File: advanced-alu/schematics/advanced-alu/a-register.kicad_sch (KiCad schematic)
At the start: 11 parts

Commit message: updated ALU design
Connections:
- net GND: now reaches U?.10 (GND)
- net GND: now also U?.8 (GND), U?.8 (GND)
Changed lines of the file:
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@@
     (pin "2")
     (pin "3")
+    (pin "4")
+    (pin "5")
+    (pin "6")
+    (pin "10")
+    (pin "8")
+    (pin "9")
+    (pin "11")
+    (pin "12")
+    (pin "13")
+    (pin "14")
+    (pin "7")
   )
   (symbol (lib_id "74xx:74LS32") (at 153.035 46.355 0) (unit 2)
@@
       (effects (font (size 1.27 1.27)) hide)
     )
-    (pin "4")
-    (pin "5")
-    (pin "6")
+    (pin "1")
+    (pin "2")
+    (pin "3")
+    (pin "4")
+    (pin "5")
+    (pin "6")
+    (pin "10")
+    (pin "8")
+    (pin "9")
+    (pin "11")
+    (pin "12")
+    (pin "13")
+    (pin "14")
+    (pin "7")
   )
   (symbol (lib_id "power:VCC") (at 109.22 93.98 0) (unit 1)
@@
     )
     (property "Datasheet" "" (id 3) (at 109.22 93.98 0)
+      (effects (font (size 1.27 1.27)) hide)
+    )
+    (pin "1")
+  )
+  (symbol (lib_id "power:GND") (at 139.065 93.98 0) (unit 1)
+    (in_bom yes) (on_board yes) (fields_autoplaced)
+    (property "Reference" "#PWR?" (id 0) (at 139.065 100.33 0)
+      (effects (font (size 1.27 1.27)) hide)
+    )
+    (property "Value" "GND" (id 1) (at 139.065 98.5425 0))
+    (property "Footprint" "" (id 2) (at 139.065 93.98 0)
+      (effects (font (size 1.27 1.27)) hide)
+    )
+    (property "Datasheet" "" (id 3) (at 139.065 93.98 0)
       (effects (font (size 1.27 1.27)) hide)
     )
@@
     (pin "1")
     (pin "2")
+    (pin "3")
+    (pin "4")
+    (pin "5")
+    (pin "6")
+    (pin "8")
+    (pin "9")
+    (pin "10")
+    (pin "11")
+    (pin "12")
+    (pin "13")
+    (pin "14")
+    (pin "7")
+  )
+  (symbol (lib_id "power:GND") (at 68.58 93.98 0) (unit 1)
+    (in_bom yes) (on_board yes) (fields_autoplaced)
+    (property "Reference" "#PWR?" (id 0) (at 68.58 100.33 0)
+      (effects (font (size 1.27 1.27)) hide)
+    )
+    (property "Value" "GND" (id 1) (at 68.58 98.5425 0))
+    (property "Footprint" "" (id 2) (at 68.58 93.98 0)
+      (effects (font (size 1.27 1.27)) hide)
+    )
+    (property "Datasheet" "" (id 3) (at 68.58 93.98 0)
+      (effects (font (size 1.27 1.27)) hide)
+    )
+    (pin "1")
   )
   (symbol (lib_id "74xx:74LS08") (at 132.08 43.815 0) (unit 4)
@@
       (effects (font (size 1.27 1.27)) hide)
     )
-    (pin "11")
-    (pin "12")
-    (pin "13")
+    (pin "1")
+    (pin "2")
+    (pin "3")
+    (pin "4")
+    (pin "5")
+    (pin "6")
+    (pin "10")
+    (pin "8")
+    (pin "9")
+    (pin "11")
+    (pin "12")
+    (pin "13")
+    (pin "14")
+    (pin "7")
   )
   (symbol (lib_id "74xx:74LS194") (at 164.465 93.98 270) (unit 1)
@@
     (pin "2")
     (pin "3")
+    (pin "4")
+    (pin "5")
+    (pin "6")
+    (pin "10")
+    (pin "8")
+    (pin "9")
+    (pin "11")
+    (pin "12")
+    (pin "13")
+    (pin "14")
+    (pin "7")
   )
   (symbol (lib_id "74xx:74LS08") (at 116.84 156.845 180) (unit 2)
@@
       (effects (font (size 1.27 1.27)) hide)
     )
-    (pin "4")
-    (pin "5")
-    (pin "6")
+    (pin "1")
+    (pin "2")
+    (pin "3")
+    (pin "4")
+    (pin "5")
+    (pin "6")
+    (pin "10")
+    (pin "8")
+    (pin "9")
+    (pin "11")
+    (pin "12")
+    (pin "13")
+    (pin "14")
+    (pin "7")
   )
   (symbol (lib_id "74xx:74LS08") (at 73.66 137.16 180) (unit 3)
@@
       (effects (font (size 1.27 1.27)) hide)
     )
-    (pin "10")
-    (pin "8")
-    (pin "9")
+    (pin "1")
+    (pin "2")
+    (pin "3")
+    (pin "4")
+    (pin "5")
+    (pin "6")
+    (pin "10")
+    (pin "8")
+    (pin "9")
+    (pin "11")
+    (pin "12")
+    (pin "13")
+    (pin "14")
+    (pin "7")
+  )
+  (symbol (lib_id "power:GND") (at 203.2 93.98 0) (unit 1)
+    (in_bom yes) (on_board yes) (fields_autoplaced)
+    (property "Reference" "#PWR?" (id 0) (at 203.2 100.33 0)
+      (effects (font (size 1.27 1.27)) hide)
+    )
+    (property "Value" "GND" (id 1) (at 203.2 98.5425 0))
+    (property "Footprint" "" (id 2) (at 203.2 93.98 0)
+      (effects (font (size 1.27 1.27)) hide)
+    )
+    (property "Datasheet" "" (id 3) (at 203.2 93.98 0)
+      (effects (font (size 1.27 1.27)) hide)
+    )
+    (pin "1")
   )
   (symbol (lib_id "74xx:74LS32") (at 94.615 151.765 180) (unit 1)
@@
     (pin "2")
     (pin "3")
+    (pin "4")
+    (pin "5")
+    (pin "6")
+    (pin "10")
+    (pin "8")
+    (pin "9")
+    (pin "11")
+    (pin "12")
+    (pin "13")
+    (pin "14")
+    (pin "7")
   )
 )

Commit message: updated documentation
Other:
- title: (none) -> Advanced Arithmetic Logic Unit - Accumulator/Shifter
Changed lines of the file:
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@@
 (kicad_sch (version 20211123) (generator eeschema)
   (paper "A4")
+  (title_block
+    (title "Advanced Arithmetic Logic Unit - Accumulator/Shifter")
+  )
   (junction (at 179.7246 106.68) (diameter 0) (color 0 0 0 0)
   )

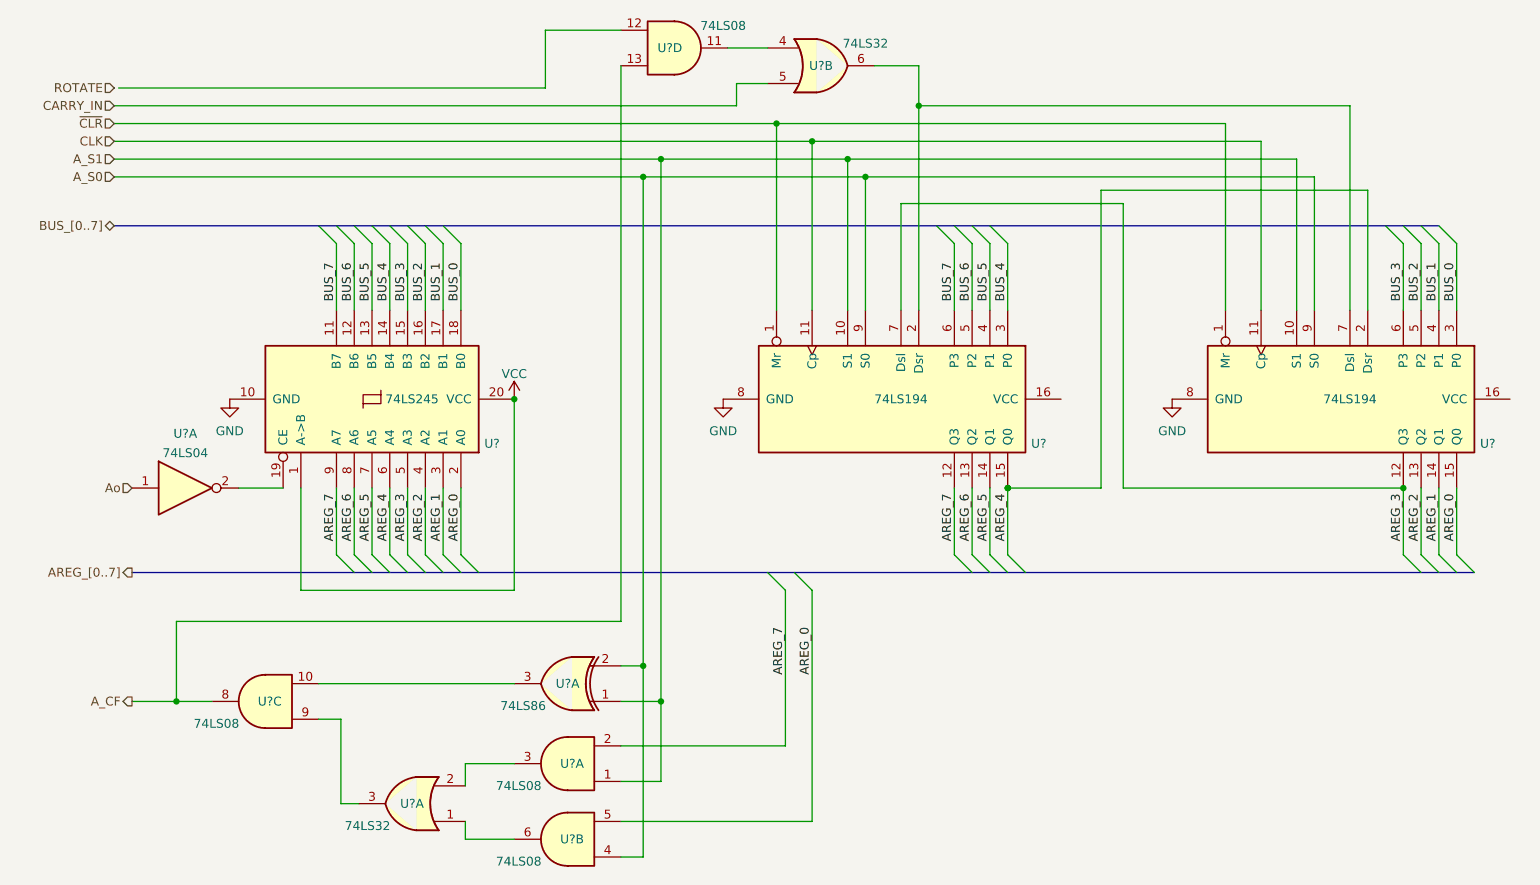
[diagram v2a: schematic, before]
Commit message: returned temp registr to being 8-bit
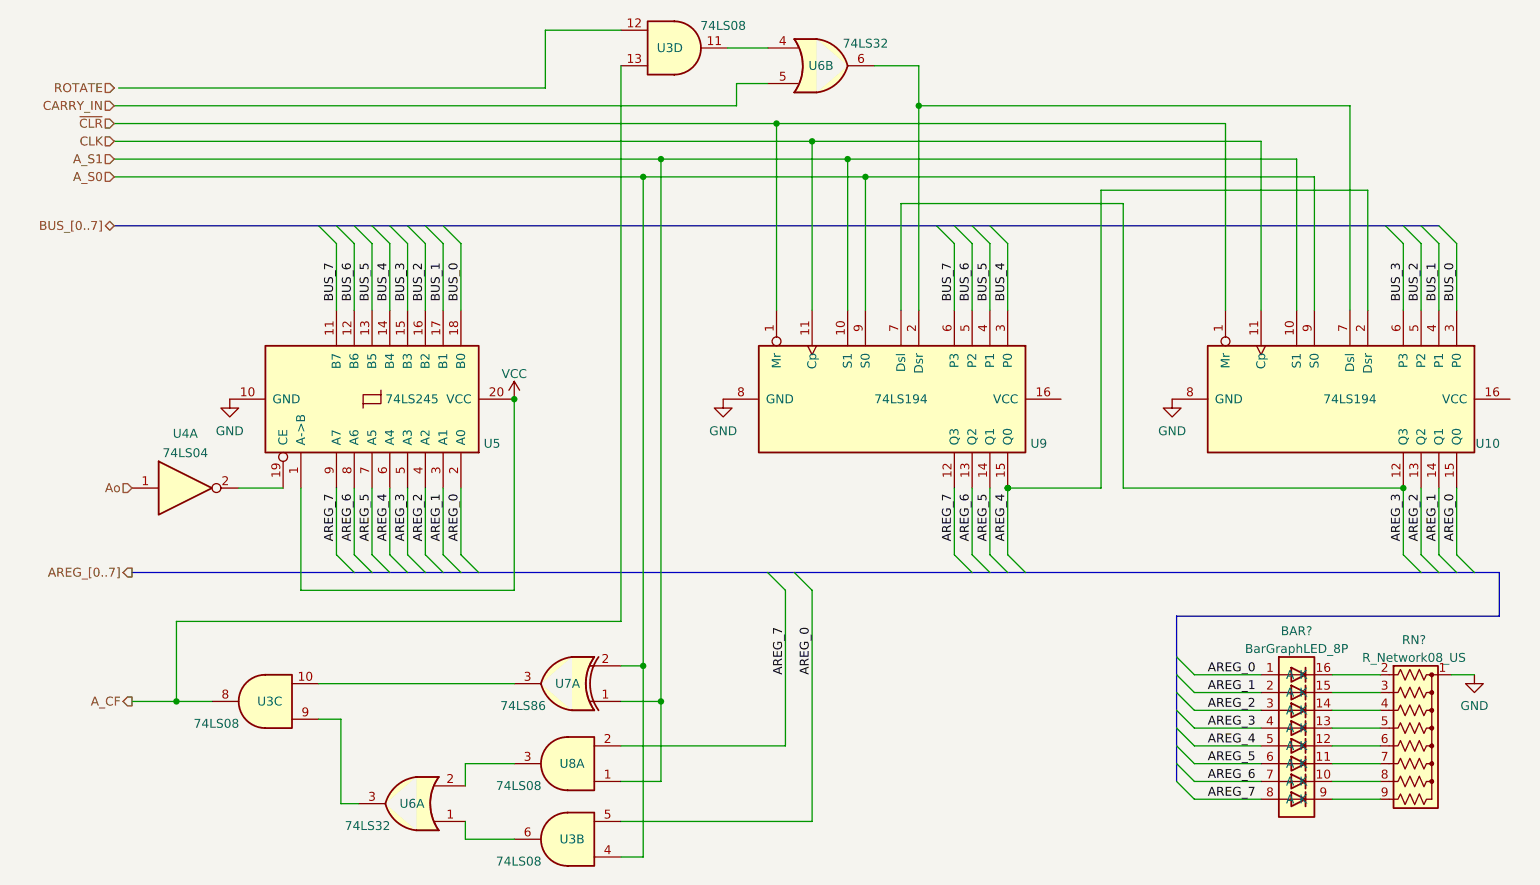
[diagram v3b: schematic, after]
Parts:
- added BAR?: BarGraphLED_8P, symbol common-symbols:BarGraphLED_8P
- added RN?: R_Network08_US, Resistor_THT:R_Array_SIP9, symbol Device:R_Network08_US
- gave numbers to parts that had none: 8
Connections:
- net AREG_0: now also BAR?.1 (A)
- net AREG_1: now also BAR?.2 (A)
- net AREG_2: now also BAR?.3 (A)
- net AREG_3: now also BAR?.4 (A)
- net AREG_4: now also BAR?.5 (A)
- net AREG_5: now also BAR?.6 (A)
- net AREG_6: now also BAR?.7 (A)
- net AREG_7: now also BAR?.8 (A)
- net GND: now also RN?.1 (common)
- new net: BAR?.10 (K), RN?.8 (R7)
- new net: BAR?.11 (K), RN?.7 (R6)
- new net: BAR?.12 (K), RN?.6 (R5)
- new net: BAR?.13 (K), RN?.5 (R4)
- new net: BAR?.14 (K), RN?.4 (R3)
- new net: BAR?.15 (K), RN?.3 (R2)
- new net: BAR?.16 (K), RN?.2 (R1)
- new net: BAR?.9 (K), RN?.9 (R8)

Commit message: small changes toimprove layout
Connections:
- net ROTATE: now also U3.12
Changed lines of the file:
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@@
     (stroke (width 0) (type default) (color 0 0 0 0))
   )
-  (wire (pts (xy 52.705 49.53) (xy 113.665 49.53))
+  (wire (pts (xy 52.07 49.53) (xy 113.665 49.53))
     (stroke (width 0) (type default) (color 0 0 0 0))
   )
@@
     (pin "2")
     (pin "3")
+  )
+  (symbol (lib_id "74xx:74LS32") (at 153.035 46.355 0) (unit 2)
+    (in_bom yes) (on_board yes)
+    (property "Reference" "U6" (id 0) (at 153.035 46.355 0))
+    (property "Value" "74LS32" (id 1) (at 159.385 43.18 0))
+    (property "Footprint" "" (id 2) (at 153.035 46.355 0)
+      (effects (font (size 1.27 1.27)) hide)
+    )
+    (property "Datasheet" "http://www.ti.com/lit/gpn/sn74LS32" (id 3) (at 153.035 46.355 0)
+      (effects (font (size 1.27 1.27)) hide)
+    )
     (pin "4")
     (pin "5")
     (pin "6")
-    (pin "10")
-    (pin "8")
-    (pin "9")
-    (pin "11")
-    (pin "12")
-    (pin "13")
-    (pin "14")
-    (pin "7")
-  )
-  (symbol (lib_id "74xx:74LS32") (at 153.035 46.355 0) (unit 2)
-    (in_bom yes) (on_board yes)
-    (property "Reference" "U6" (id 0) (at 153.035 46.355 0))
-    (property "Value" "74LS32" (id 1) (at 159.385 43.18 0))
-    (property "Footprint" "" (id 2) (at 153.035 46.355 0)
-      (effects (font (size 1.27 1.27)) hide)
-    )
-    (property "Datasheet" "http://www.ti.com/lit/gpn/sn74LS32" (id 3) (at 153.035 46.355 0)
-      (effects (font (size 1.27 1.27)) hide)
-    )
-    (pin "1")
-    (pin "2")
-    (pin "3")
-    (pin "4")
-    (pin "5")
-    (pin "6")
-    (pin "10")
-    (pin "8")
-    (pin "9")
-    (pin "11")
-    (pin "12")
-    (pin "13")
-    (pin "14")
-    (pin "7")
   )
   (symbol (lib_id "power:VCC") (at 109.22 93.98 0) (unit 1)
@@
     (pin "1")
     (pin "2")
-    (pin "3")
-    (pin "4")
-    (pin "5")
-    (pin "6")
-    (pin "8")
-    (pin "9")
-    (pin "10")
+  )
+  (symbol (lib_id "power:GND") (at 68.58 93.98 0) (unit 1)
+    (in_bom yes) (on_board yes) (fields_autoplaced)
+    (property "Reference" "#PWR03" (id 0) (at 68.58 100.33 0)
+      (effects (font (size 1.27 1.27)) hide)
+    )
+    (property "Value" "GND" (id 1) (at 68.58 98.5425 0))
+    (property "Footprint" "" (id 2) (at 68.58 93.98 0)
+      (effects (font (size 1.27 1.27)) hide)
+    )
+    (property "Datasheet" "" (id 3) (at 68.58 93.98 0)
+      (effects (font (size 1.27 1.27)) hide)
+    )
+    (pin "1")
+  )
+  (symbol (lib_id "74xx:74LS08") (at 132.08 43.815 0) (unit 4)
+    (in_bom yes) (on_board yes)
+    (property "Reference" "U3" (id 0) (at 131.445 43.815 0))
+    (property "Value" "74LS08" (id 1) (at 139.065 40.64 0))
+    (property "Footprint" "" (id 2) (at 132.08 43.815 0)
+      (effects (font (size 1.27 1.27)) hide)
+    )
+    (property "Datasheet" "http://www.ti.com/lit/gpn/sn74LS08" (id 3) (at 132.08 43.815 0)
+      (effects (font (size 1.27 1.27)) hide)
+    )
     (pin "11")
     (pin "12")
     (pin "13")
-    (pin "14")
-    (pin "7")
-  )
-  (symbol (lib_id "power:GND") (at 68.58 93.98 0) (unit 1)
-    (in_bom yes) (on_board yes) (fields_autoplaced)
-    (property "Reference" "#PWR03" (id 0) (at 68.58 100.33 0)
-      (effects (font (size 1.27 1.27)) hide)
-    )
-    (property "Value" "GND" (id 1) (at 68.58 98.5425 0))
-    (property "Footprint" "" (id 2) (at 68.58 93.98 0)
-      (effects (font (size 1.27 1.27)) hide)
-    )
-    (property "Datasheet" "" (id 3) (at 68.58 93.98 0)
-      (effects (font (size 1.27 1.27)) hide)
-    )
-    (pin "1")
-  )
-  (symbol (lib_id "74xx:74LS08") (at 132.08 43.815 0) (unit 4)
-    (in_bom yes) (on_board yes)
-    (property "Reference" "U3" (id 0) (at 131.445 43.815 0))
-    (property "Value" "74LS08" (id 1) (at 139.065 40.64 0))
-    (property "Footprint" "" (id 2) (at 132.08 43.815 0)
-      (effects (font (size 1.27 1.27)) hide)
-    )
-    (property "Datasheet" "http://www.ti.com/lit/gpn/sn74LS08" (id 3) (at 132.08 43.815 0)
-      (effects (font (size 1.27 1.27)) hide)
-    )
-    (pin "1")
-    (pin "2")
-    (pin "3")
-    (pin "4")
-    (pin "5")
-    (pin "6")
-    (pin "10")
-    (pin "8")
-    (pin "9")
-    (pin "11")
-    (pin "12")
-    (pin "13")
-    (pin "14")
-    (pin "7")
   )
   (symbol (lib_id "74xx:74LS194") (at 164.465 93.98 270) (unit 1)
@@
     (pin "2")
     (pin "3")
+  )
+  (symbol (lib_id "74xx:74LS08") (at 116.84 156.845 180) (unit 2)
+    (in_bom yes) (on_board yes)
+    (property "Reference" "U3" (id 0) (at 117.475 156.845 0))
+    (property "Value" "74LS08" (id 1) (at 109.855 160.02 0))
+    (property "Footprint" "" (id 2) (at 116.84 156.845 0)
+      (effects (font (size 1.27 1.27)) hide)
+    )
+    (property "Datasheet" "http://www.ti.com/lit/gpn/sn74LS08" (id 3) (at 116.84 156.845 0)
+      (effects (font (size 1.27 1.27)) hide)
+    )
     (pin "4")
     (pin "5")
     (pin "6")
+  )
+  (symbol (lib_id "power:GND") (at 246.38 133.35 0) (unit 1)
+    (in_bom yes) (on_board yes) (fields_autoplaced)
+    (property "Reference" "#PWR?" (id 0) (at 246.38 139.7 0)
+      (effects (font (size 1.27 1.27)) hide)
+    )
+    (property "Value" "GND" (id 1) (at 246.38 137.7934 0))
+    (property "Footprint" "" (id 2) (at 246.38 133.35 0)
+      (effects (font (size 1.27 1.27)) hide)
+    )
+    (property "Datasheet" "" (id 3) (at 246.38 133.35 0)
+      (effects (font (size 1.27 1.27)) hide)
+    )
+    (pin "1")
+  )
+  (symbol (lib_id "74xx:74LS08") (at 73.66 137.16 180) (unit 3)
+    (in_bom yes) (on_board yes)
+    (property "Reference" "U3" (id 0) (at 74.295 137.16 0))
+    (property "Value" "74LS08" (id 1) (at 66.675 140.335 0))
+    (property "Footprint" "" (id 2) (at 73.66 137.16 0)
+      (effects (font (size 1.27 1.27)) hide)
+    )
+    (property "Datasheet" "http://www.ti.com/lit/gpn/sn74LS08" (id 3) (at 73.66 137.16 0)
+      (effects (font (size 1.27 1.27)) hide)
+    )
     (pin "10")
     (pin "8")
     (pin "9")
-    (pin "11")
-    (pin "12")
-    (pin "13")
-    (pin "14")
-    (pin "7")
-  )
-  (symbol (lib_id "74xx:74LS08") (at 116.84 156.845 180) (unit 2)
-    (in_bom yes) (on_board yes)
-    (property "Reference" "U3" (id 0) (at 117.475 156.845 0))
-    (property "Value" "74LS08" (id 1) (at 109.855 160.02 0))
-    (property "Footprint" "" (id 2) (at 116.84 156.845 0)
-      (effects (font (size 1.27 1.27)) hide)
-    )
-    (property "Datasheet" "http://www.ti.com/lit/gpn/sn74LS08" (id 3) (at 116.84 156.845 0)
-      (effects (font (size 1.27 1.27)) hide)
-    )
-    (pin "1")
-    (pin "2")
-    (pin "3")
-    (pin "4")
-    (pin "5")
-    (pin "6")
-    (pin "10")
-    (pin "8")
-    (pin "9")
-    (pin "11")
-    (pin "12")
-    (pin "13")
-    (pin "14")
-    (pin "7")
-  )
-  (symbol (lib_id "power:GND") (at 246.38 133.35 0) (unit 1)
-    (in_bom yes) (on_board yes) (fields_autoplaced)
-    (property "Reference" "#PWR?" (id 0) (at 246.38 139.7 0)
-      (effects (font (size 1.27 1.27)) hide)
-    )
-    (property "Value" "GND" (id 1) (at 246.38 137.7934 0))
-    (property "Footprint" "" (id 2) (at 246.38 133.35 0)
-      (effects (font (size 1.27 1.27)) hide)
-    )
-    (property "Datasheet" "" (id 3) (at 246.38 133.35 0)
-      (effects (font (size 1.27 1.27)) hide)
-    )
-    (pin "1")
-  )
-  (symbol (lib_id "74xx:74LS08") (at 73.66 137.16 180) (unit 3)
-    (in_bom yes) (on_board yes)
-    (property "Reference" "U3" (id 0) (at 74.295 137.16 0))
-    (property "Value" "74LS08" (id 1) (at 66.675 140.335 0))
-    (property "Footprint" "" (id 2) (at 73.66 137.16 0)
-      (effects (font (size 1.27 1.27)) hide)
-    )
-    (property "Datasheet" "http://www.ti.com/lit/gpn/sn74LS08" (id 3) (at 73.66 137.16 0)
-      (effects (font (size 1.27 1.27)) hide)
-    )
-    (pin "1")
-    (pin "2")
-    (pin "3")
-    (pin "4")
-    (pin "5")
-    (pin "6")
-    (pin "10")
-    (pin "8")
-    (pin "9")
-    (pin "11")
-    (pin "12")
-    (pin "13")
-    (pin "14")
-    (pin "7")
   )
   (symbol (lib_id "power:GND") (at 203.2 93.98 0) (unit 1)
@@
     (pin "2")
     (pin "3")
-    (pin "4")
-    (pin "5")
-    (pin "6")
-    (pin "10")
-    (pin "8")
-    (pin "9")
-    (pin "11")
-    (pin "12")
-    (pin "13")
-    (pin "14")
-    (pin "7")
   )
 )
